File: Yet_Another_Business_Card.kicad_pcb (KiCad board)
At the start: 2 copper layers, 85 x 54 mm, 412 parts, among them U1 STM32F103C8Tx

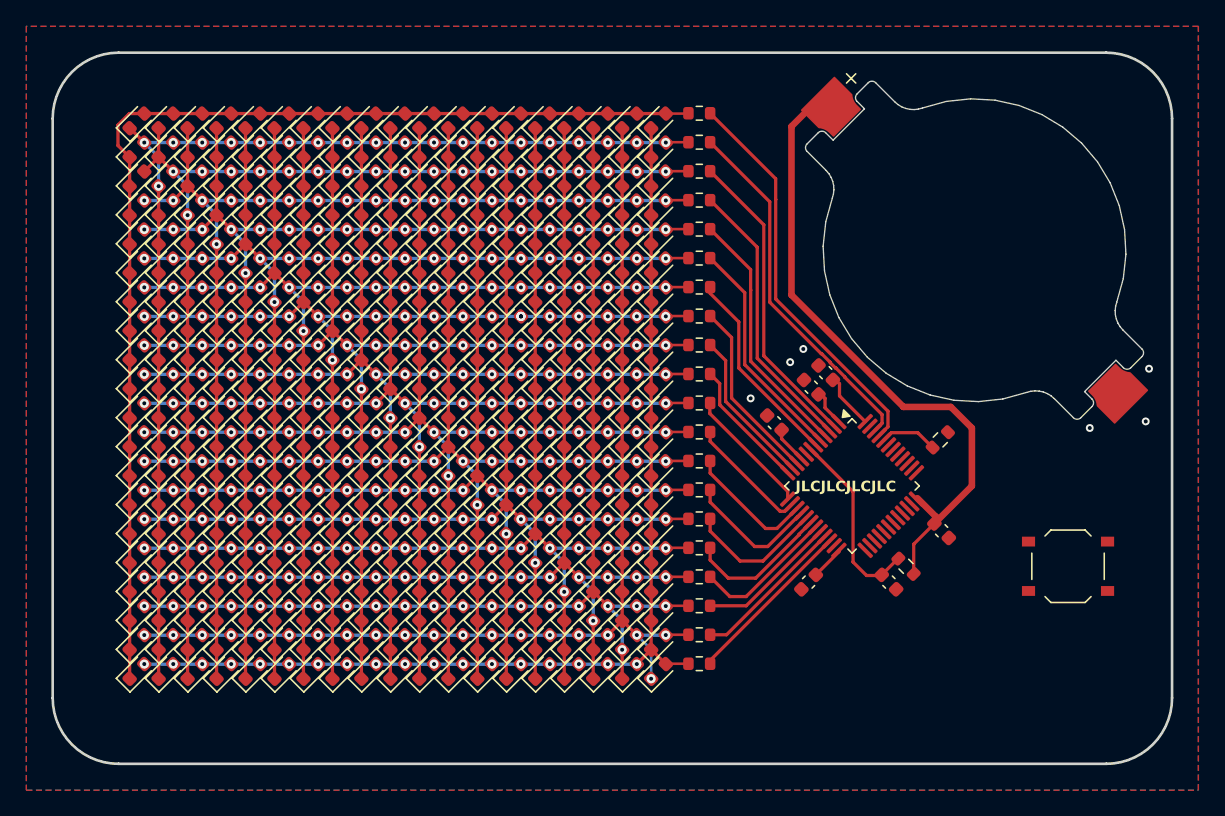
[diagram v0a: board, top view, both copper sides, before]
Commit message: Added SWDIO connector, python script to convert gif to matrix data
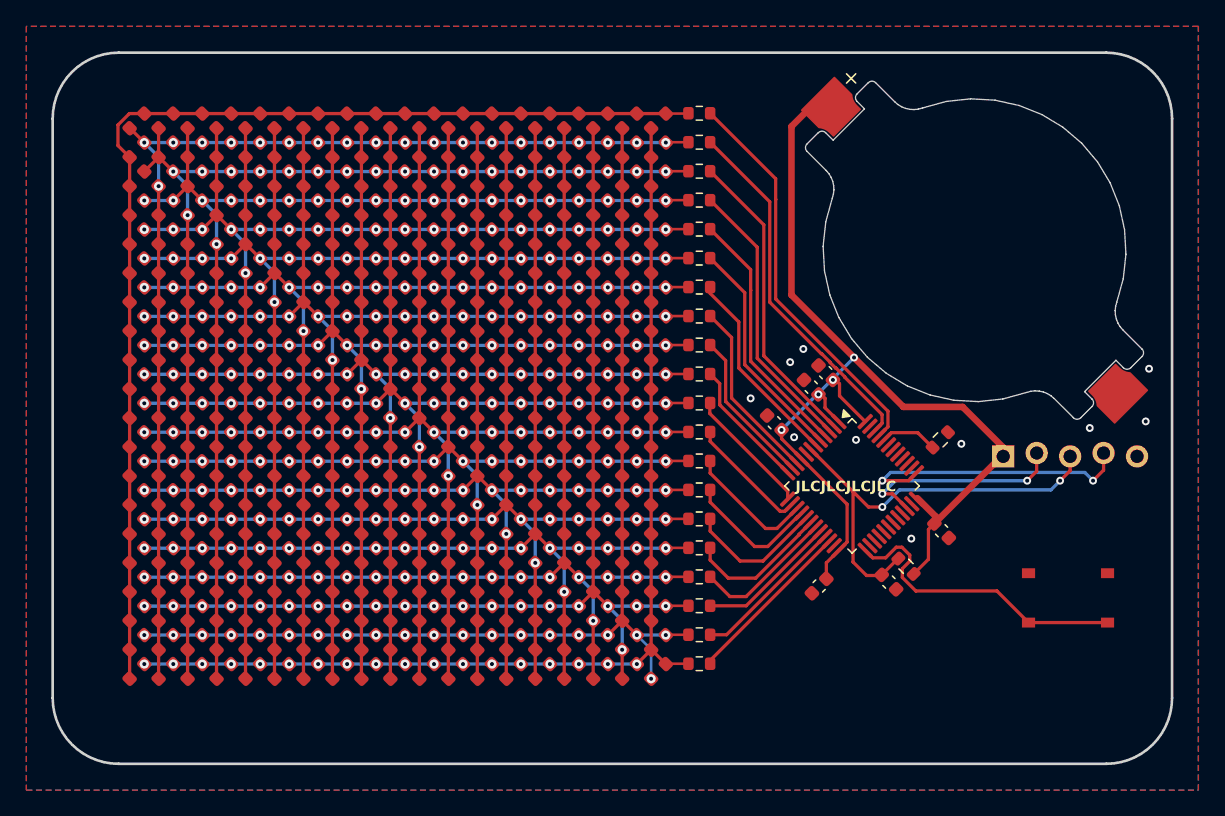
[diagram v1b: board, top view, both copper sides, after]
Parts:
- added G***: LOGO, LOGO, B.Cu at (148.2, 84.0)
- added J1: Conn_01x05_Socket, Connector_PinSocket_2.54mm:PinSocket_1x05_P2.54mm_Vertical, F.Cu at (193.4, 87.8)
- D10, D100, D101, D102, D103, D104, D105, D106, D107, D108, D109, D11, D110, D111, D112, D113, D114, D115, D116, D117, D118, D119, D12, D120, D121, D122, D123, D124, D125, D126, D127, D128, D129, D13, D130, D131, D132, D133, D134, D135, D136, D137, D138, D139, D14, D140, D141, D142, D143, D144, D145, D146, D147, D148, D149, D15, D150, D151, D152, D153, D154, D155, D156, D157, D158, D159, D16, D160, D161, D162, D163, D164, D165, D166, D167, D168, D169, D17, D170, D171, D172, D173, D174, D175, D176, D177, D178, D179, D18, D180, D181, D182, D183, D184, D185, D186, D187, D188, D189, D19, D190, D191, D192, D193, D194, D195, D196, D197, D198, D199, D2, D20, D200, D201, D202, D203, D204, D205, D206, D207, D208, D209, D21, D210, D211, D212, D213, D214, D215, D216, D217, D218, D219, D22, D220, D221, D222, D223, D224, D225, D226, D227, D228, D229, D23, D230, D231, D232, D233, D234, D235, D236, D237, D238, D239, D24, D240, D241, D242, D243, D244, D245, D246, D247, D248, D249, D25, D250, D251, D252, D253, D254, D255, D256, D257, D258, D259, D26, D260, D261, D262, D263, D264, D265, D266, D267, D268, D269, D27, D270, D271, D272, D273, D274, D275, D276, D277, D278, D279, D28, D280, D281, D282, D283, D284, D285, D286, D287, D288, D289, D29, D290, D291, D292, D293, D294, D295, D296, D297, D298, D299, D3, D30, D300, D301, D302, D303, D304, D305, D306, D307, D308, D309, D31, D310, D311, D312, D313, D314, D315, D316, D317, D318, D319, D32, D320, D321, D322, D323, D324, D325, D326, D327, D328, D329, D33, D330, D331, D332, D333, D334, D335, D336, D337, D338, D339, D34, D340, D341, D342, D343, D344, D345, D346, D347, D348, D349, D35, D350, D351, D352, D353, D354, D355, D356, D357, D358, D359, D36, D360, D361, D362, D363, D364, D365, D366, D367, D368, D369, D37, D370, D371, D372, D373, D374, D375, D376, D377, D378, D379, D38, D380, D381, D39, D4, D40, D41, D42, D43, D44, D45, D46, D47, D48, D49, D5, D50, D51, D52, D53, D54, D55, D56, D57, D58, D59, D6, D60, D61, D62, D63, D64, D65, D66, D67, D68, D69, D7, D70, D71, D72, D73, D74, D75, D76, D77, D78, D79, D8, D80, D81, D82, D83, D84, D85, D86, D87, D88, D89, D9, D90, D91, D92, D93, D94, D95, D96, D97, D98, D99: footprint LED_SMD:LED_0603_1608Metric -> Business_card_footprints:LED_0603_no_silkscreen
- moved G*** 13.9 mm to (198.9, 104.2)
- moved BTN_MAIN1 2.40 mm to (198.3, 98.7)
- moved C4 0.85 mm to (179.4, 97.8)
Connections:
- U1 pad 34: unconnected-(U1-PA13-Pad34) -> SWDIO
- U1 pad 37: unconnected-(U1-PA14-Pad37) -> SWCLK
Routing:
- net BTN_MAIN_PIN: track 0.00 -> 23.1 mm
- net SWCLK: track 0.00 -> 21.8 mm, vias 0 -> 2
- net MCU_NRST: track 14.3 -> 33.5 mm, vias 0 -> 2
- net VDD: track 62.5 -> 81.6 mm, vias 0 -> 4
- net SWDIO: track 0.00 -> 16.2 mm, vias 0 -> 2
- net GND: vias 6 -> 10
- net CHRLY_8: vias 21 -> 20
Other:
- board text added: "Made by: Andrea Massetti In: a room full of Post-it With: a lot of coffee"
- board text removed: "Made by: Andrea Massetti In: Turin With: a lot of coffee"

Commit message: Updated firmware, PCB files are updated after the second prototype production (added just 2 battery holder footprints as a test)
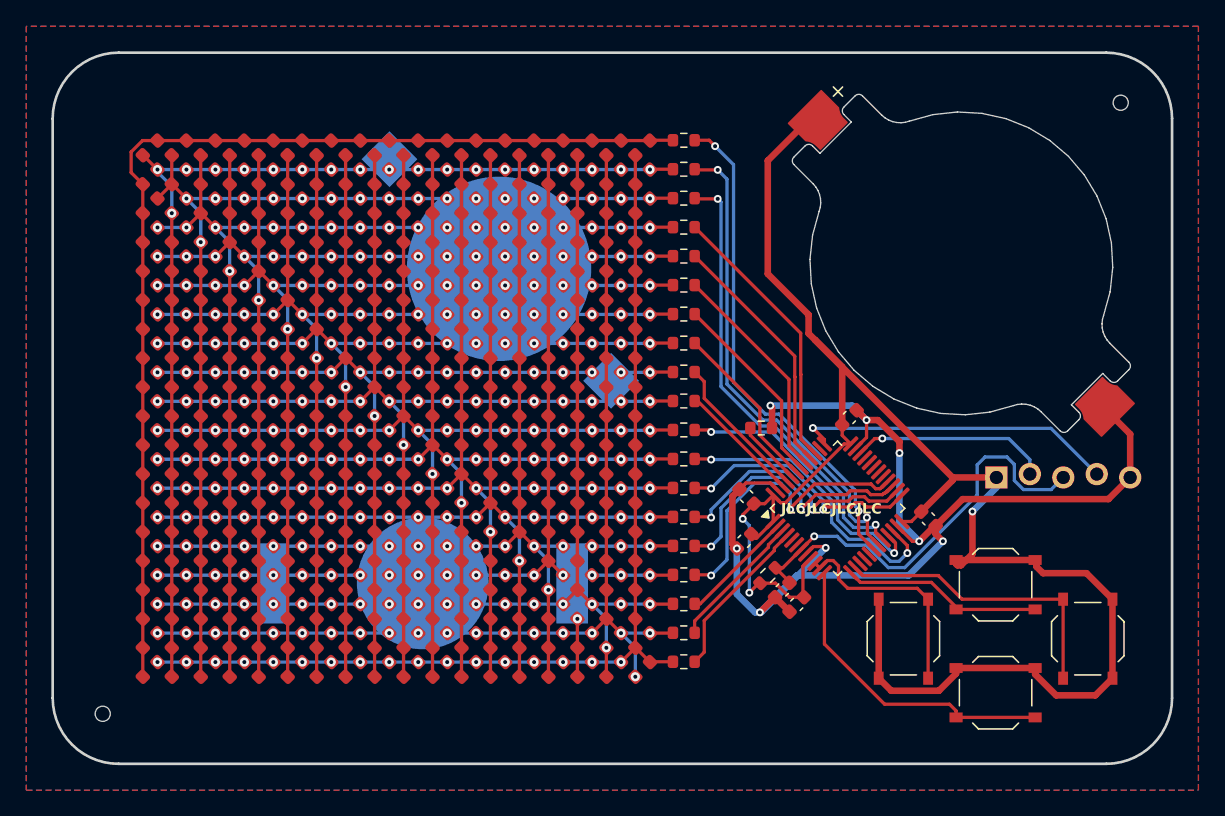
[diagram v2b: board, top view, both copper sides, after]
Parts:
- removed the D115 at (167.2, 73.5)
- removed the D134 at (167.2, 75.7)
- removed the D153 at (167.2, 77.9)
- removed the D172 at (167.2, 80.1)
- removed the D191 at (167.2, 82.3)
- removed the D20 at (167.2, 62.5)
- removed the D210 at (167.2, 84.5)
- removed the D229 at (167.2, 86.7)
- removed the D248 at (167.2, 88.9)
- removed the D267 at (167.2, 91.1)
- removed the D286 at (167.2, 93.3)
- removed the D305 at (167.2, 95.5)
- removed the D324 at (167.2, 97.7)
- removed D343, D362, D363, D364, D365, D366, D367, D368, D369, D370, D371, D372, D373, D374, D375, D376, D377, D378, D379, D380, D381: LED, Business_card_footprints:LED_0603_no_silkscreen
- removed the D39 at (167.2, 64.7)
- removed the D58 at (167.2, 66.9)
- removed the D77 at (167.2, 69.1)
- removed the D96 at (167.2, 71.3)
- removed the G*** at (148.2, 84.0)
- removed the R12 at (170.3, 81.7)
- removed the R13 at (170.3, 83.9)
- removed the R14 at (170.3, 86.1)
- removed the R15 at (170.3, 88.3)
- removed the R17 at (170.3, 92.7)
- added BTN_MAIN3: SW_Push, Business_card_footprints:SW_Push_1P1T_XKB_TS-1187A, F.Cu at (185.8, 101.8)
- added BTN_MAIN4: SW_Push, Business_card_footprints:SW_Push_1P1T_XKB_TS-1187A, F.Cu at (199.8, 101.8)
- added BTN_MAIN5: SW_Push, Business_card_footprints:SW_Push_1P1T_XKB_TS-1187A, F.Cu at (192.8, 105.9)
- added G***: LOGO, LOGO, B.Cu at (148.3, 84.2)
- added G***: LOGO, LOGO, B.Cu at (173.2, 106.8)
- added R18: 47, Resistor_SMD:R_0603_1608Metric, F.Cu at (169.1, 92.5)
- added R19: 47, Resistor_SMD:R_0603_1608Metric, F.Cu at (169.1, 94.8)
- added R20: 47, Resistor_SMD:R_0603_1608Metric, F.Cu at (169.1, 97.0)
- added R7: 47, Resistor_SMD:R_0603_1608Metric, F.Cu at (169.1, 70.5)
- added REF**: BAT-SMD_CR2032-3V, Stratobotic_EasyEda:BAT-SMD_CR2032-3V, B.Cu at (155.2, 73.8)
- added REF**: BAT-SMD_MY-2032-12, Stratobotic_EasyEda:BAT-SMD_MY-2032-12, B.Cu at (149.3, 97.6)
- BTN_MAIN1: footprint Button_Switch_SMD:SW_Push_1P1T_XKB_TS-1187A -> Business_card_footprints:SW_Push_1P1T_XKB_TS-1187A
- moved R1 32.9 mm to (169.1, 99.2)
- moved R2 32.9 mm to (169.1, 101.3)
- moved R3 32.9 mm to (169.1, 103.5)
- moved R4 31.0 mm to (169.1, 64.0)
- moved R6 31.0 mm to (169.1, 68.3)
- moved R5 31.0 mm to (169.1, 66.2)
- moved R13 19.7 mm to (169.1, 83.8)
- moved R12 19.7 mm to (169.1, 81.5)
- moved R14 15.6 mm to (169.1, 86.0)
- moved R15 15.6 mm to (169.1, 88.2)
- moved C2 13.9 mm to (177.7, 99.2), turned to -135 degrees
- moved R21 13.6 mm to (175.0, 85.8), turned to 0 degrees
- moved C4 12.8 mm to (173.7, 94.4), turned to -135 degrees
- moved C3 11.2 mm to (173.9, 91.0)
- moved C6 11.1 mm to (181.7, 85.0), turned to 45 degrees
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- renumbered C6 to C1, C1 to C2, C2 to C3, C3 to C4, C4 to C5, C5 to C6, D2 to D1, D11 to D10, D106 to D100, D107 to D101, D108 to D102, D109 to D103, D110 to D104, D111 to D105, D112 to D106, D113 to D107, D114 to D108, D116 to D109, D12 to D11, D117 to D110, D118 to D111, D119 to D112, D120 to D113, D121 to D114, D122 to D115, D123 to D116, D124 to D117, D125 to D118, D126 to D119, D13 to D12, D127 to D120, D128 to D121, D129 to D122, D130 to D123, D131 to D124, D132 to D125, D133 to D126, D135 to D127, D136 to D128, D137 to D129, D14 to D13, D138 to D130, D139 to D131, D140 to D132, D141 to D133, D142 to D134, D143 to D135, D144 to D136, D145 to D137, D146 to D138, D147 to D139, D15 to D14, D148 to D140, D149 to D141, D150 to D142, D151 to D143, D152 to D144, D154 to D145, D155 to D146, D156 to D147, D157 to D148, D158 to D149, D16 to D15, D159 to D150, D160 to D151, D161 to D152, D162 to D153, D163 to D154, D164 to D155, D165 to D156, D166 to D157, D167 to D158, D168 to D159, D17 to D16, D169 to D160, D170 to D161, D171 to D162, D173 to D163, D174 to D164, D175 to D165, D176 to D166, D177 to D167, D178 to D168, D179 to D169, D18 to D17, D180 to D170, D181 to D171, D182 to D172, D183 to D173, D184 to D174, D185 to D175, D186 to D176, D187 to D177, D188 to D178, D189 to D179, D19 to D18, D190 to D180, D192 to D181, D193 to D182, D194 to D183, D195 to D184, D196 to D185, D197 to D186, D198 to D187, D199 to D188, D200 to D189, D21 to D19, D201 to D190, D202 to D191, D203 to D192, D204 to D193, D205 to D194, D206 to D195, D207 to D196, D208 to D197, D209 to D198, D211 to D199, D3 to D2, D22 to D20, D212 to D200, D213 to D201, D214 to D202, D215 to D203, D216 to D204, D217 to D205, D218 to D206, D219 to D207, D220 to D208, D221 to D209, D23 to D21, D222 to D210, D223 to D211, D224 to D212, D225 to D213, D226 to D214, D227 to D215, D228 to D216, D230 to D217, D231 to D218, D232 to D219, D24 to D22, D233 to D220, D234 to D221, D235 to D222, D236 to D223, D237 to D224, D238 to D225, D239 to D226, D240 to D227, D241 to D228, D242 to D229, D25 to D23, D243 to D230, D244 to D231, D245 to D232, D246 to D233, D247 to D234, D249 to D235, D250 to D236, D251 to D237, D252 to D238, D253 to D239, D26 to D24, D254 to D240, D255 to D241, D256 to D242, D257 to D243, D258 to D244, D259 to D245, D260 to D246, D261 to D247, D262 to D248, D263 to D249, D27 to D25, D264 to D250, D265 to D251, D266 to D252, D268 to D253, D269 to D254, D270 to D255, D271 to D256, D272 to D257, D273 to D258, D274 to D259, D28 to D26, D275 to D260, D276 to D261, D277 to D262, D278 to D263, D279 to D264, D280 to D265, D281 to D266, D282 to D267, D283 to D268, D284 to D269, D29 to D27, D285 to D270, D287 to D271, D288 to D272, D289 to D273, D290 to D274, D291 to D275, D292 to D276, D293 to D277, D294 to D278, D295 to D279, D30 to D28, D296 to D280, D297 to D281, D298 to D282, D299 to D283, D300 to D284, D301 to D285, D302 to D286, D303 to D287, D304 to D288, D306 to D289, D31 to D29, D307 to D290, D308 to D291, D309 to D292, D310 to D293, D311 to D294, D312 to D295, D313 to D296, D314 to D297, D315 to D298, D316 to D299, D4 to D3, D32 to D30, D317 to D300, D318 to D301, D319 to D302, D320 to D303, D321 to D304, D322 to D305, D323 to D306, D325 to D307, D326 to D308, D327 to D309, D33 to D31, D328 to D310, D329 to D311, D330 to D312, D331 to D313, D332 to D314, D333 to D315, D334 to D316, D335 to D317, D336 to D318, D337 to D319, D34 to D32, D338 to D320, D339 to D321, D340 to D322, D341 to D323, D342 to D324, D344 to D325, D345 to D326, D346 to D327, D347 to D328, D348 to D329, D35 to D33, D349 to D330, D350 to D331, D351 to D332, D352 to D333, D353 to D334, D354 to D335, D355 to D336, D356 to D337, D357 to D338, D358 to D339, D36 to D34, D359 to D340, D360 to D341, D361 to D342, D37 to D35, D38 to D36, D40 to D37, D41 to D38, D42 to D39, D5 to D4, D43 to D40, D44 to D41, D45 to D42, D46 to D43, D47 to D44, D48 to D45, D49 to D46, D50 to D47, D51 to D48, D52 to D49, D6 to D5, D53 to D50, D54 to D51, D55 to D52, D56 to D53, D57 to D54, D59 to D55, D60 to D56, D61 to D57, D62 to D58, D63 to D59, D7 to D6, D64 to D60, D65 to D61, D66 to D62, D67 to D63, D68 to D64, D69 to D65, D70 to D66, D71 to D67, D72 to D68, D73 to D69, D8 to D7, D74 to D70, D75 to D71, D76 to D72, D78 to D73, D79 to D74, D80 to D75, D81 to D76, D82 to D77, D83 to D78, D84 to D79, D9 to D8, D85 to D80, D86 to D81, D87 to D82, D88 to D83, D89 to D84, D90 to D85, D91 to D86, D92 to D87, D93 to D88, D94 to D89, D10 to D9, D95 to D90, D97 to D91, D98 to D92, D99 to D93, D100 to D94, D101 to D95, D102 to D96, D103 to D97, D104 to D98, D105 to D99, R5 to R1, R1 to R12, R2 to R13, R3 to R14, R4 to R15, R21 to R17, R6 to R2, R22 to R21, R7 to R3, R18 to R4, R19 to R5, R20 to R6
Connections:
- BTN_MAIN1 pad 1: GND -> VDD
- BTN_MAIN1 pad 2: BTN_MAIN_PIN -> BTN_UP_PIN
- R1 pad 1: CHRLY_3 -> CHRLY_17
- R10 pad 1: /PA0_CL -> CHRLY_7
- R10 pad 2: CHRLY_8 -> /PB6_CL
- R11 pad 1: /PA1_CL -> CHRLY_8
- R11 pad 2: CHRLY_9 -> /PB7_CL
- R12 pad 1: CHRLY_1 -> CHRLY_9
- R13 pad 1: CHRLY_2 -> CHRLY_10
- R14 pad 1: CHRLY_19 -> CHRLY_11
- R15 pad 1: CHRLY_20 -> CHRLY_12
- R16 pad 1: /PA6_CL -> CHRLY_13
- R16 pad 2: CHRLY_14 -> /PB12_CL
- R2 pad 1: CHRLY_4 -> CHRLY_18
- R3 pad 1: CHRLY_5 -> CHRLY_19
- R4 pad 1: CHRLY_16 -> CHRLY_1
- R5 pad 1: CHRLY_17 -> CHRLY_2
- R6 pad 1: CHRLY_18 -> CHRLY_3
- R8 pad 1: CHRLY_6 -> CHRLY_5
- R8 pad 2: /PD0_CL -> /PB4_CL
- R9 pad 1: CHRLY_7 -> CHRLY_6
- R9 pad 2: /PD1_CL -> /PB5_CL
- U1 pad 10: /PA0_CL -> BTN_SX_PIN
- U1 pad 11: /PA1_CL -> BTN_SX_PIN
- U1 pad 12: /PA2_CL -> BTN_DOWN_PIN
- U1 pad 13: /PA3_CL -> BTN_UP_PIN
- U1 pad 14: /PA4_CL -> BTN_DX_PIN
- U1 pad 15: /PA5_CL -> unconnected-(U1-PA5-Pad15)
- U1 pad 16: /PA6_CL -> unconnected-(U1-PA6-Pad16)
- U1 pad 17: /PA7_CL -> unconnected-(U1-PA7-Pad17)
- U1 pad 25: BTN_MAIN_PIN -> /PB12_CL
- U1 pad 26: unconnected-(U1-PB13-Pad26) -> /PB13_CL
- U1 pad 27: unconnected-(U1-PB14-Pad27) -> /PB14_CL
- U1 pad 28: unconnected-(U1-PB15-Pad28) -> /PB15_CL
- U1 pad 39: unconnected-(U1-PB3-Pad39) -> /PB3_CL
- U1 pad 40: unconnected-(U1-PB4-Pad40) -> /PB4_CL
- U1 pad 41: unconnected-(U1-PB5-Pad41) -> /PB5_CL
- U1 pad 42: unconnected-(U1-PB6-Pad42) -> /PB6_CL
- U1 pad 43: unconnected-(U1-PB7-Pad43) -> /PB7_CL
- U1 pad 5: /PD0_CL -> unconnected-(U1-PD0-Pad5)
- U1 pad 6: /PD1_CL -> unconnected-(U1-PD1-Pad6)
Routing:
- net GND: track 0.00 -> 94.6 mm, vias 10 -> 8
- net CHRLY_20: track 81.8 -> 0.00 mm, vias 18 -> 0
- net VDD: track 81.6 -> 136.9 mm, vias 4 -> 3
- net /PB0_CL: track 10.9 -> 38.0 mm, vias 0 -> 2
- net /PB1_CL: track 10.8 -> 36.9 mm, vias 0 -> 2
- net /PB2_CL: track 10.7 -> 34.8 mm, vias 0 -> 2
- net BTN_DOWN_PIN: track 0.00 -> 24.0 mm
- net BTN_MAIN_PIN: track 23.1 -> 0.00 mm
- net BTN_DX_PIN: track 0.00 -> 22.8 mm
- net /PB15_CL: track 0.00 -> 22.6 mm, vias 0 -> 2
- net /PB14_CL: track 0.00 -> 21.2 mm, vias 0 -> 2
- net /PB3_CL: track 0.00 -> 21.0 mm
- net /PB13_CL: track 0.00 -> 19.8 mm, vias 0 -> 2
- net /PB8_CL: track 30.3 -> 11.2 mm
- net /PB12_CL: track 0.00 -> 19.0 mm, vias 0 -> 2
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- added copper zone on B.Cu, net (none)
- added copper zone on F.Cu, net (none)
- removed copper zone on B.Cu, net GND
- removed copper zone on F.Cu, net GND
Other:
- outline, holes or cut-outs redrawn
- board text added: "Made by: Andrea G. Massetti In: a room full of Post-it (TO) With: a lot of coffee and some"
- board text removed: "Made by: Andrea Massetti In: a room full of Post-it With: a lot of coffee"
- board text removed: "PUSH ME!"

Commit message: Flashed code to second board of hw v2, ordered hw v3 boards
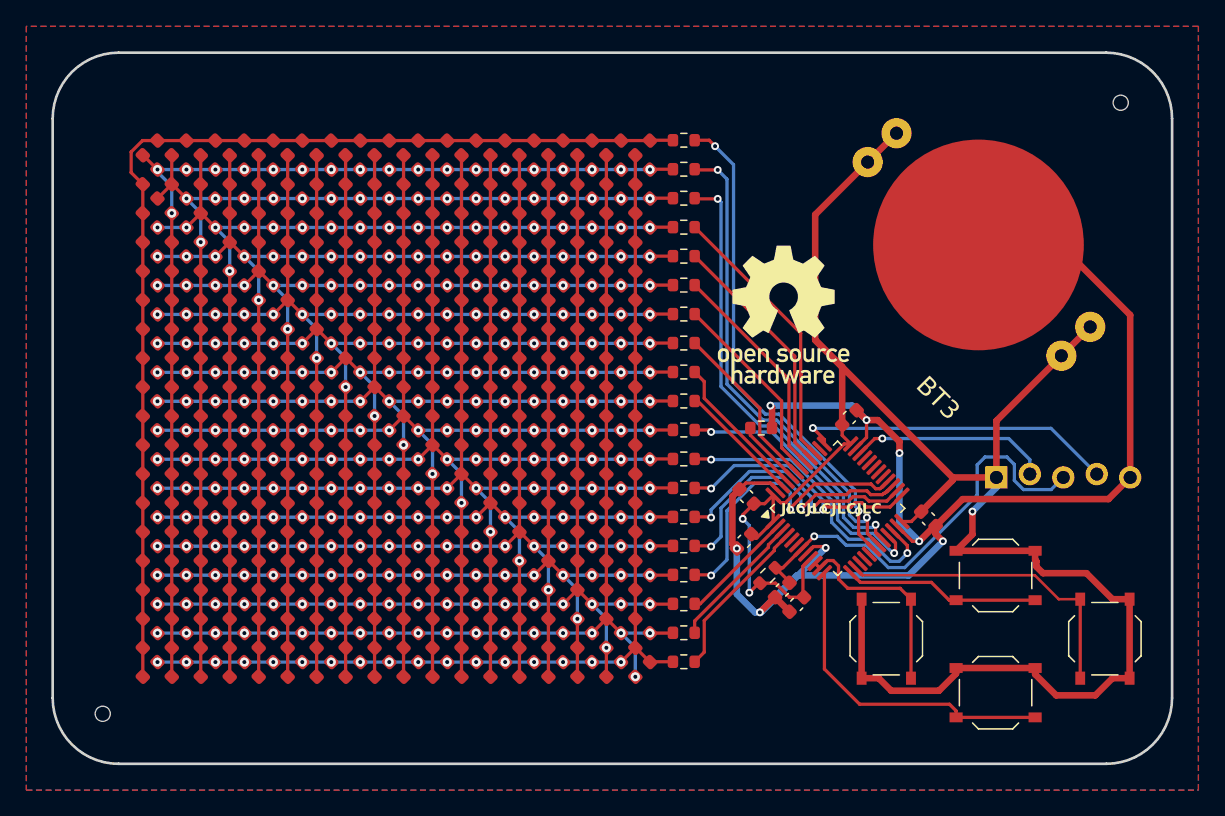
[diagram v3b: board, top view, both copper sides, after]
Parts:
- removed BT1: 1057, Battery:BatteryHolder_Keystone_1057_1x2032
- removed the G*** at (196.4, 96.7)
- removed REF**: BAT-SMD_CR2032-3V, Stratobotic_EasyEda:BAT-SMD_CR2032-3V
- removed REF**: BAT-SMD_MY-2032-12, Stratobotic_EasyEda:BAT-SMD_MY-2032-12
- added BT3: BAT-HLD-001-THM, Stratobotic_custom:BAT_BAT-HLD-001-THM, F.Cu at (191.5, 71.9)
- added G***: LOGO, LOGO, F.Cu at (176.7, 77.2)
- added G***: LOGO, LOGO, B.Cu at (184.2, 79.2)
- added G***: LOGO, LOGO, B.Cu at (188.9, 69.4)
- G***: moved to F.Cu
- moved BTN_MAIN3 1.30 mm to (184.5, 101.8)
- moved BTN_MAIN4 1.30 mm to (201.1, 101.8)
- moved BTN_MAIN1 0.70 mm to (192.8, 97.0)
- turned G*** to 0 degrees
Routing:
- net GND: track 94.6 -> 114.6 mm
- net VDD: track 136.9 -> 152.1 mm
- net BTN_SX_PIN: track 16.8 -> 15.5 mm
- net BTN_DX_PIN: track 22.8 -> 24.1 mm
- net BTN_DOWN_PIN: track 24.0 -> 25.1 mm
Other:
- board text added: "+"
- board text added: "-"
- board text added: "TCK"
- board text added: "TMS"
- board text added: "Yet Another Business Card"
- board text added: "firmware v?.?"
- board text added: "hardware v3.0"
- board text added: "nRST"
